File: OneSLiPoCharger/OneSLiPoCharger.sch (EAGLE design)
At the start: 16 parts, among them IC1 LM358N, Q1 BUZ10

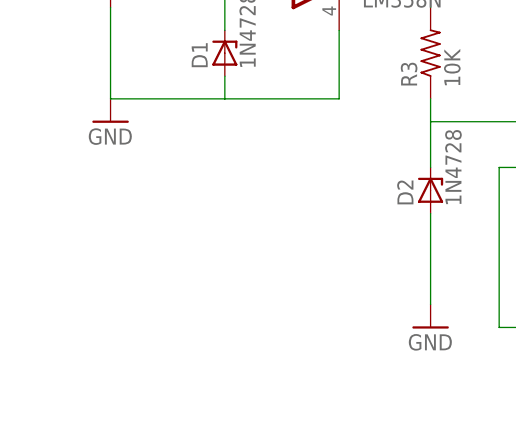
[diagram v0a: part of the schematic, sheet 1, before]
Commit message: Add XT60 to schematic
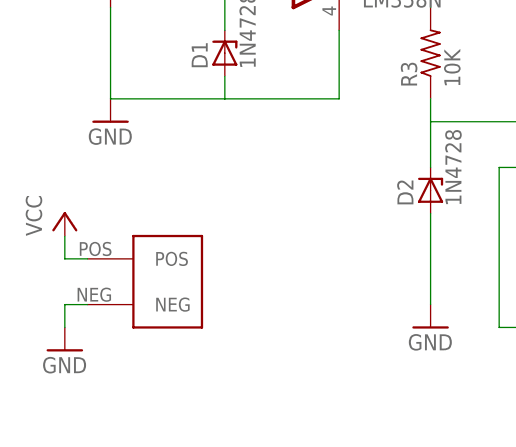
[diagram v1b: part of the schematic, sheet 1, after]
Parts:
- added U$3: XT60, XTConnector:XT60
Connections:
- net GND: now also U$3.NEG
- net VCC: now also U$3.POS
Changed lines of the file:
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@@
 <part name="C3" library="rcl" deviceset="C-US" device="C0805" value="4.7uF"/>
 <part name="GND6" library="supply1" deviceset="GND" device=""/>
+<part name="U$3" library="XTConnector" deviceset="XT60" device=""/>
+<part name="GND7" library="supply1" deviceset="GND" device=""/>
+<part name="P+5" library="supply1" deviceset="VCC" device=""/>
 </parts>
 <sheets>
@@
 <instance part="P+2" gate="VCC" x="101.6" y="33.02"/>
 <instance part="P+3" gate="1" x="116.84" y="27.94"/>
+<instance part="U$3" gate="G$1" x="20.32" y="5.08"/>
+<instance part="GND7" gate="1" x="17.78" y="-2.54"/>
+<instance part="P+5" gate="VCC" x="17.78" y="12.7"/>
 </instances>
 <busses>
@@
 <wire x1="101.6" y1="25.4" x2="101.6" y2="30.48" width="0.1524" layer="91"/>
 </segment>
+<segment>
+<pinref part="P+5" gate="VCC" pin="VCC"/>
+<pinref part="U$3" gate="G$1" pin="POS"/>
+<wire x1="17.78" y1="10.16" x2="17.78" y2="7.62" width="0.1524" layer="91"/>
+<wire x1="17.78" y1="7.62" x2="20.32" y2="7.62" width="0.1524" layer="91"/>
+</segment>
 </net>
 <net name="GND" class="0">
@@
 <wire x1="109.22" y1="-5.08" x2="109.22" y2="0" width="0.1524" layer="91"/>
 </segment>
+<segment>
+<pinref part="U$3" gate="G$1" pin="NEG"/>
+<pinref part="GND7" gate="1" pin="GND"/>
+<wire x1="20.32" y1="2.54" x2="17.78" y2="2.54" width="0.1524" layer="91"/>
+<wire x1="17.78" y1="2.54" x2="17.78" y2="0" width="0.1524" layer="91"/>
+</segment>
 </net>

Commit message: Start laying out the board
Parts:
- added LED2: (no value), led:LED3MM
- added R7: 3.9k, rcl:R-US_M0805
- R5: value (none) -> 4.7K; device rcl:R-US_M0805 -> rcl:R-US_0411/12
- R6: value 3.9k -> (none)
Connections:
- new net N$10: LED1.A, R5.1
- net +5V: now also LED2.A, R5.2; no longer LED1.A
- net GND: now also LED1.C, R7.1, U$2.P$1; no longer R6.1
- net N$6: now also LED2.C, R6.2; no longer LED1.C, R5.2
- net N$7: now also R6.1; no longer R5.1
- net N$8: now also R7.2; no longer R6.2
- net N$9: now also U$2.P$2
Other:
- moved on the sheet: R6
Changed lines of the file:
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@@
 <part name="U$1" library="MCP73831" deviceset="MCP73831" device=""/>
 <part name="P+4" library="supply1" deviceset="+5V" device=""/>
-<part name="LED1" library="led" deviceset="LED" device="3MM"/>
+<part name="LED2" library="led" deviceset="LED" device="3MM"/>
 <part name="C2" library="rcl" deviceset="C-US" device="C0805" value="4.7uF"/>
-<part name="R5" library="rcl" deviceset="R-US_" device="M0805"/>
+<part name="R6" library="rcl" deviceset="R-US_" device="M0805"/>
 <part name="GND4" library="supply1" deviceset="GND" device=""/>
 <part name="GND5" library="supply1" deviceset="GND" device=""/>
-<part name="R6" library="rcl" deviceset="R-US_" device="M0805" value="3.9k"/>
+<part name="R7" library="rcl" deviceset="R-US_" device="M0805" value="3.9k"/>
 <part name="U$2" library="Picoblade" deviceset="PICOBLADE-2PIN" device=""/>
 <part name="C3" library="rcl" deviceset="C-US" device="C0805" value="4.7uF"/>
@@
 <part name="GND7" library="supply1" deviceset="GND" device=""/>
 <part name="P+5" library="supply1" deviceset="VCC" device=""/>
+<part name="LED1" library="led" deviceset="LED" device="3MM"/>
+<part name="R5" library="rcl" deviceset="R-US_" device="0411/12" value="4.7K"/>
+<part name="P+6" library="supply1" deviceset="+5V" device=""/>
+<part name="GND8" library="supply1" deviceset="GND" device=""/>
 </parts>
 <sheets>
@@
 <instance part="GND7" gate="1" x="17.78" y="-2.54"/>
 <instance part="P+5" gate="VCC" x="17.78" y="12.7"/>
+<instance part="LED1" gate="G$1" x="88.9" y="50.8" rot="R90"/>
+<instance part="R5" gate="G$1" x="78.74" y="50.8" rot="R180"/>
+<instance part="P+6" gate="1" x="68.58" y="55.88"/>
+<instance part="GND8" gate="1" x="96.52" y="45.72"/>
 </instances>
 <busses>
@@
 <wire x1="17.78" y1="2.54" x2="17.78" y2="0" width="0.1524" layer="91"/>
 </segment>
+<segment>
+<pinref part="LED1" gate="G$1" pin="C"/>
+<pinref part="GND8" gate="1" pin="GND"/>
+<wire x1="93.98" y1="50.8" x2="96.52" y2="50.8" width="0.1524" layer="91"/>
+<wire x1="96.52" y1="50.8" x2="96.52" y2="48.26" width="0.1524" layer="91"/>
+</segment>
 </net>
 <net name="N$1" class="0">
@@
 <wire x1="116.84" y1="20.32" x2="116.84" y2="25.4" width="0.1524" layer="91"/>
 </segment>
+<segment>
+<pinref part="P+6" gate="1" pin="+5V"/>
+<pinref part="R5" gate="G$1" pin="2"/>
+<wire x1="68.58" y1="53.34" x2="68.58" y2="50.8" width="0.1524" layer="91"/>
+<wire x1="68.58" y1="50.8" x2="73.66" y2="50.8" width="0.1524" layer="91"/>
+</segment>
+</net>
+<net name="N$10" class="0">
+<segment>
+<pinref part="R5" gate="G$1" pin="1"/>
+<pinref part="LED1" gate="G$1" pin="A"/>
+<wire x1="83.82" y1="50.8" x2="86.36" y2="50.8" width="0.1524" layer="91"/>
+</segment>
 </net>
 </nets>
@@
 <instance part="U$1" gate="G$1" x="35.56" y="48.26"/>
 <instance part="P+4" gate="1" x="7.62" y="58.42"/>
-<instance part="LED1" gate="G$1" x="15.24" y="48.26"/>
+<instance part="LED2" gate="G$1" x="15.24" y="48.26"/>
 <instance part="C2" gate="G$1" x="7.62" y="48.26"/>
-<instance part="R5" gate="G$1" x="15.24" y="35.56" rot="R90"/>
+<instance part="R6" gate="G$1" x="15.24" y="35.56" rot="R90"/>
 <instance part="GND4" gate="1" x="7.62" y="38.1"/>
 <instance part="GND5" gate="1" x="48.26" y="33.02"/>
-<instance part="R6" gate="G$1" x="48.26" y="43.18" rot="R90"/>
+<instance part="R7" gate="G$1" x="48.26" y="43.18" rot="R90"/>
 <instance part="U$2" gate="G$1" x="58.42" y="55.88" rot="R180"/>
 <instance part="C3" gate="G$1" x="43.18" y="63.5"/>
@@
 <net name="+5V" class="0">
 <segment>
-<pinref part="LED1" gate="G$1" pin="A"/>
+<pinref part="LED2" gate="G$1" pin="A"/>
 <wire x1="15.24" y1="50.8" x2="15.24" y2="53.34" width="0.1524" layer="91"/>
 <pinref part="C2" gate="G$1" pin="1"/>
@@
 <net name="N$6" class="0">
 <segment>
-<pinref part="LED1" gate="G$1" pin="C"/>
-<pinref part="R5" gate="G$1" pin="2"/>
+<pinref part="LED2" gate="G$1" pin="C"/>
+<pinref part="R6" gate="G$1" pin="2"/>
 <wire x1="15.24" y1="43.18" x2="15.24" y2="40.64" width="0.1524" layer="91"/>
 </segment>
@@
 <net name="N$7" class="0">
 <segment>
-<pinref part="R5" gate="G$1" pin="1"/>
+<pinref part="R6" gate="G$1" pin="1"/>
 <wire x1="15.24" y1="30.48" x2="20.32" y2="30.48" width="0.1524" layer="91"/>
 <wire x1="20.32" y1="30.48" x2="20.32" y2="43.18" width="0.1524" layer="91"/>
@@
 </segment>
 <segment>
-<pinref part="R6" gate="G$1" pin="1"/>
+<pinref part="R7" gate="G$1" pin="1"/>
 <wire x1="43.18" y1="38.1" x2="48.26" y2="38.1" width="0.1524" layer="91"/>
 <pinref part="GND5" gate="1" pin="GND"/>
@@
 <pinref part="C3" gate="G$1" pin="1"/>
 <wire x1="43.18" y1="68.58" x2="43.18" y2="66.04" width="0.1524" layer="91"/>
-<wire x1="43.18" y1="66.04" x2="53.34" y2="66.04" width="0.1524" layer="91"/>
-<wire x1="53.34" y1="66.04" x2="53.34" y2="58.42" width="0.1524" layer="91"/>
+<wire x1="43.18" y1="66.04" x2="50.8" y2="66.04" width="0.1524" layer="91"/>
+<pinref part="U$2" gate="G$1" pin="P$1"/>
+<wire x1="50.8" y1="66.04" x2="50.8" y2="58.42" width="0.1524" layer="91"/>
 </segment>
 </net>
@@
 <segment>
 <pinref part="U$1" gate="G$1" pin="PROG"/>
-<pinref part="R6" gate="G$1" pin="2"/>
+<pinref part="R7" gate="G$1" pin="2"/>
 <wire x1="43.18" y1="48.26" x2="48.26" y2="48.26" width="0.1524" layer="91"/>
 </segment>
@@
 <pinref part="U$1" gate="G$1" pin="VBAT"/>
 <wire x1="43.18" y1="58.42" x2="43.18" y2="53.34" width="0.1524" layer="91"/>
-<wire x1="43.18" y1="53.34" x2="53.34" y2="53.34" width="0.1524" layer="91"/>
-</segment>
-</net>
+<pinref part="U$2" gate="G$1" pin="P$2"/>
+<wire x1="43.18" y1="53.34" x2="50.8" y2="53.34" width="0.1524" layer="91"/>
+</segment>
+</net>

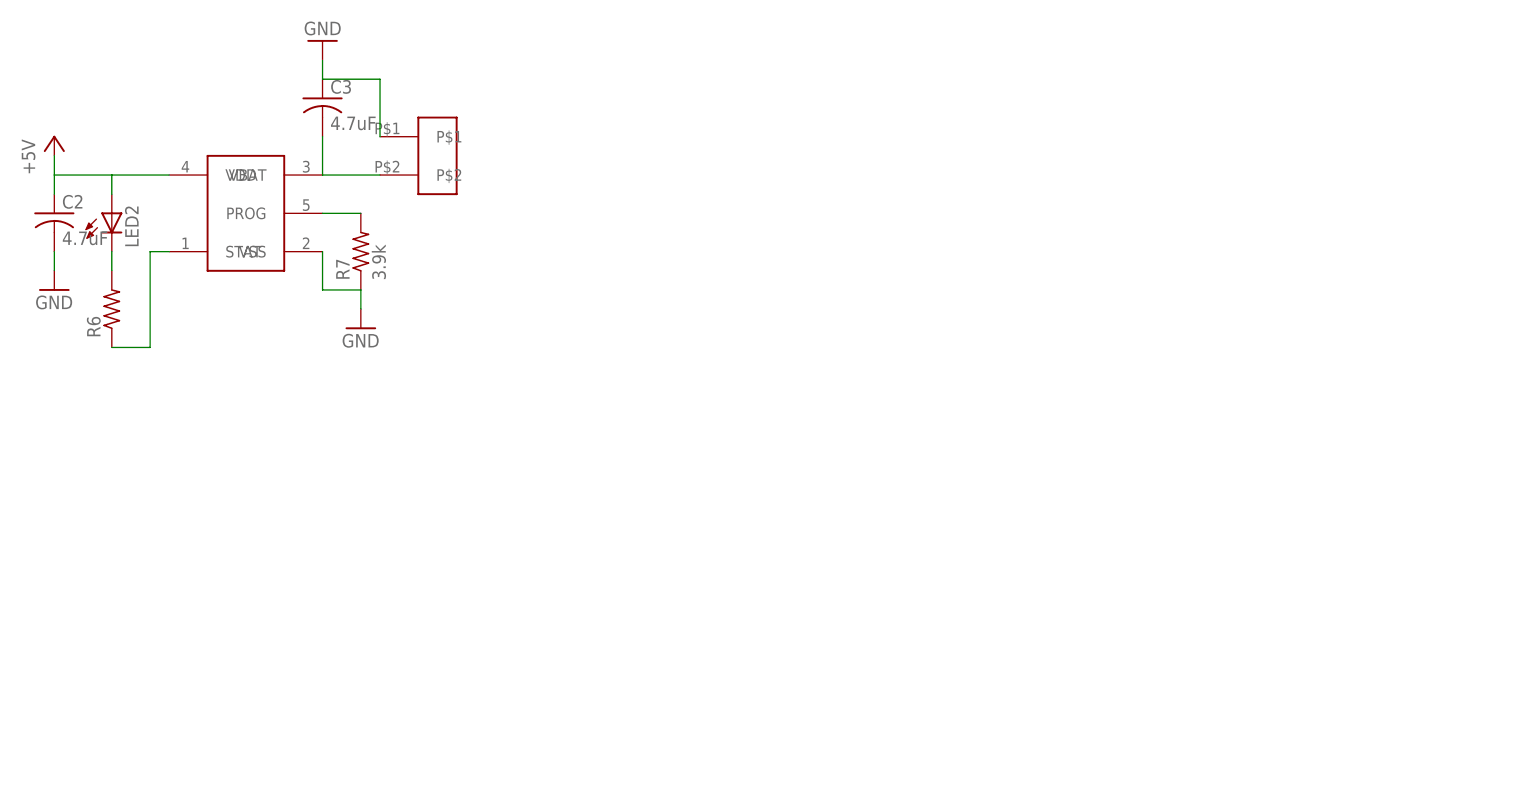
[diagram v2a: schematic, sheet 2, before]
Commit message: Add all charger circuits
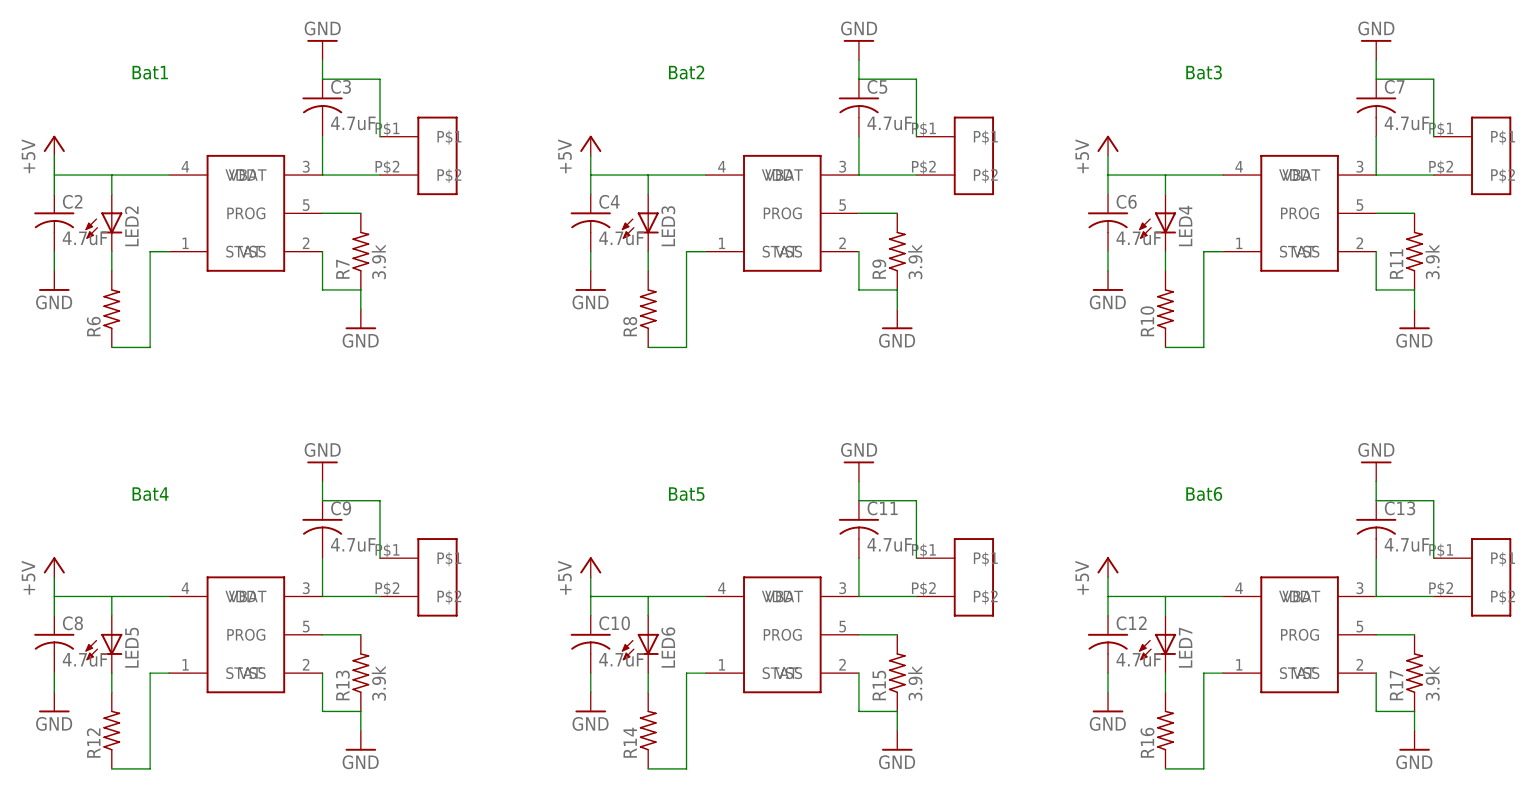
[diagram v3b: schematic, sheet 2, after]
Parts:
- added C10, C11, C12, C13, C4, C5, C6, C7, C8, C9: 4.7uF, rcl:C-USC0805
- added LED3, LED4, LED5, LED6, LED7: (no value), led:LED3MM
- added R10, R12, R14, R16, R8: (no value), rcl:R-US_M0805
- added R11, R13, R15, R17, R9: 3.9k, rcl:R-US_M0805
- added U$10, U$12, U$4, U$6, U$8: MCP73831, MCP73831:MCP73831
- added U$11, U$13, U$5, U$7, U$9: PICOBLADE-2PIN, Picoblade:PICOBLADE-2PIN
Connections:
- new net N$11: LED3.C, R8.2
- new net N$12: R8.1, U$4.STAT
- new net N$13: R9.2, U$4.PROG
- new net N$14: C5.2, U$4.VBAT, U$5.P$2
- new net N$15: LED4.C, R10.2
- new net N$16: R10.1, U$6.STAT
- new net N$17: R11.2, U$6.PROG
- new net N$18: C7.2, U$6.VBAT, U$7.P$2
- new net N$19: LED5.C, R12.2
- new net N$20: R12.1, U$8.STAT
- new net N$21: R13.2, U$8.PROG
- new net N$22: C9.2, U$8.VBAT, U$9.P$2
- new net N$23: LED6.C, R14.2
- new net N$24: R14.1, U$10.STAT
- new net N$25: R15.2, U$10.PROG
- new net N$26: C11.2, U$10.VBAT, U$11.P$2
- new net N$27: LED7.C, R16.2
- new net N$28: R16.1, U$12.STAT
- new net N$29: R17.2, U$12.PROG
- new net N$30: C13.2, U$12.VBAT, U$13.P$2
- net +5V: now also C10.1, C12.1, C4.1, C6.1, C8.1, LED3.A, LED4.A, LED5.A, LED6.A, LED7.A, U$10.VDD, U$12.VDD, U$4.VDD, U$6.VDD, U$8.VDD
- net GND: now also C10.2, C11.1, C12.2, C13.1, C4.2, C5.1, C6.2, C7.1, C8.2, C9.1, R11.1, R13.1, R15.1, R17.1, R9.1, U$10.VSS, U$11.P$1, U$12.VSS, U$13.P$1, U$4.VSS, U$5.P$1, U$6.VSS, U$7.P$1, U$8.VSS, U$9.P$1
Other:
- note added: "Bat1"
- note added: "Bat2"
- note added: "Bat3"
- note added: "Bat4"
- note added: "Bat5"
- note added: "Bat6"

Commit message: Schematic update.
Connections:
- net GND renamed N$50
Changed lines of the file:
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@@
 </segment>
 </net>
-<net name="GND" class="0">
+<net name="N$50" class="0">
 <segment>
 <pinref part="R1" gate="G$1" pin="A"/>
@@
 </segment>
 </net>
-<net name="GND" class="0">
+<net name="N$50" class="0">
 <segment>
 <pinref part="C2" gate="G$1" pin="2"/>

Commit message: Pull in updates to Picoblade library
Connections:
- net N$50 renamed GND
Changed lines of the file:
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@@
 </segment>
 </net>
-<net name="N$50" class="0">
+<net name="GND" class="0">
 <segment>
 <pinref part="R1" gate="G$1" pin="A"/>
@@
 </segment>
 </net>
-<net name="N$50" class="0">
+<net name="GND" class="0">
 <segment>
 <pinref part="C2" gate="G$1" pin="2"/>

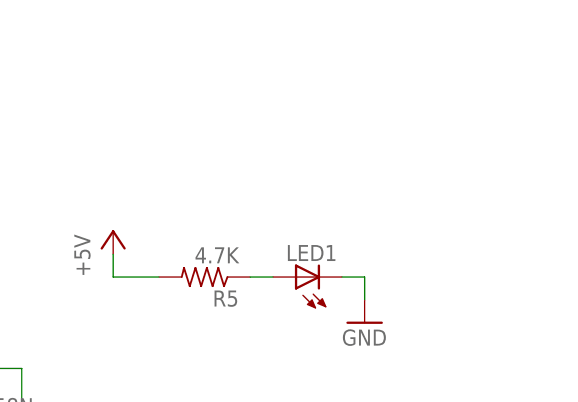
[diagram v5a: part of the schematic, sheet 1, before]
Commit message: Add a header for a voltmeter module.
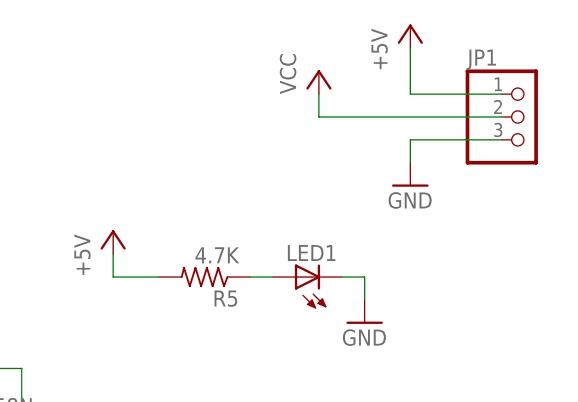
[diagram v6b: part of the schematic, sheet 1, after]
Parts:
- added JP1: (no value), pinhead:PINHD-1X3
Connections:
- net +5V: now also JP1.1
- net GND: now also JP1.3
- net VCC: now also JP1.2
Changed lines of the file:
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@@
 <part name="C13" library="rcl" deviceset="C-US" device="C0805" value="4.7uF"/>
 <part name="GND23" library="supply1" deviceset="GND" device=""/>
+<part name="JP1" library="pinhead" deviceset="PINHD-1X3" device=""/>
+<part name="GND24" library="supply1" deviceset="GND" device=""/>
+<part name="P+12" library="supply1" deviceset="+5V" device=""/>
+<part name="P+13" library="supply1" deviceset="VCC" device=""/>
 </parts>
 <sheets>
@@
 <instance part="P+6" gate="1" x="68.58" y="55.88"/>
 <instance part="GND8" gate="1" x="96.52" y="45.72"/>
+<instance part="JP1" gate="A" x="114.3" y="68.58"/>
+<instance part="GND24" gate="1" x="101.6" y="60.96"/>
+<instance part="P+12" gate="1" x="101.6" y="78.74"/>
+<instance part="P+13" gate="VCC" x="91.44" y="73.66"/>
 </instances>
 <busses>
@@
 <wire x1="17.78" y1="10.16" x2="17.78" y2="7.62" width="0.1524" layer="91"/>
 <wire x1="17.78" y1="7.62" x2="20.32" y2="7.62" width="0.1524" layer="91"/>
+</segment>
+<segment>
+<pinref part="JP1" gate="A" pin="2"/>
+<pinref part="P+13" gate="VCC" pin="VCC"/>
+<wire x1="111.76" y1="68.58" x2="91.44" y2="68.58" width="0.1524" layer="91"/>
+<wire x1="91.44" y1="68.58" x2="91.44" y2="71.12" width="0.1524" layer="91"/>
 </segment>
 </net>
@@
 <wire x1="93.98" y1="50.8" x2="96.52" y2="50.8" width="0.1524" layer="91"/>
 <wire x1="96.52" y1="50.8" x2="96.52" y2="48.26" width="0.1524" layer="91"/>
+</segment>
+<segment>
+<pinref part="JP1" gate="A" pin="3"/>
+<pinref part="GND24" gate="1" pin="GND"/>
+<wire x1="111.76" y1="66.04" x2="101.6" y2="66.04" width="0.1524" layer="91"/>
+<wire x1="101.6" y1="66.04" x2="101.6" y2="63.5" width="0.1524" layer="91"/>
 </segment>
 </net>
@@
 <wire x1="68.58" y1="50.8" x2="73.66" y2="50.8" width="0.1524" layer="91"/>
 </segment>
+<segment>
+<pinref part="P+12" gate="1" pin="+5V"/>
+<wire x1="101.6" y1="76.2" x2="101.6" y2="71.12" width="0.1524" layer="91"/>
+<pinref part="JP1" gate="A" pin="1"/>
+<wire x1="101.6" y1="71.12" x2="111.76" y2="71.12" width="0.1524" layer="91"/>
+</segment>
 </net>

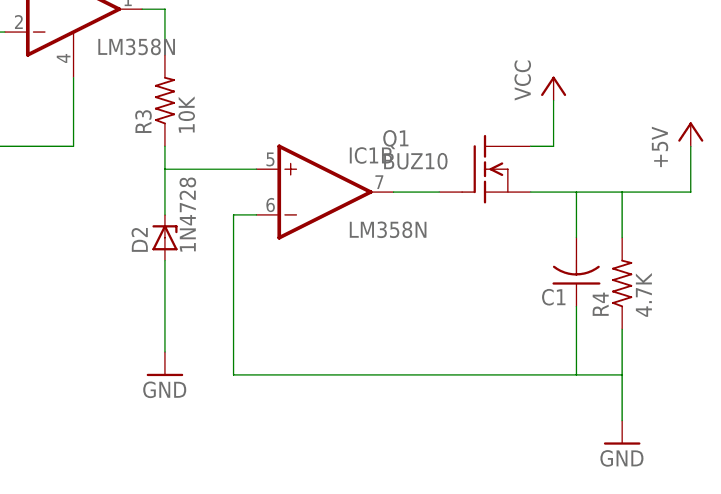
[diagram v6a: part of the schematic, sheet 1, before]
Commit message: Prep board for OSHPark. Fix feedback on voltage regulator opamp.
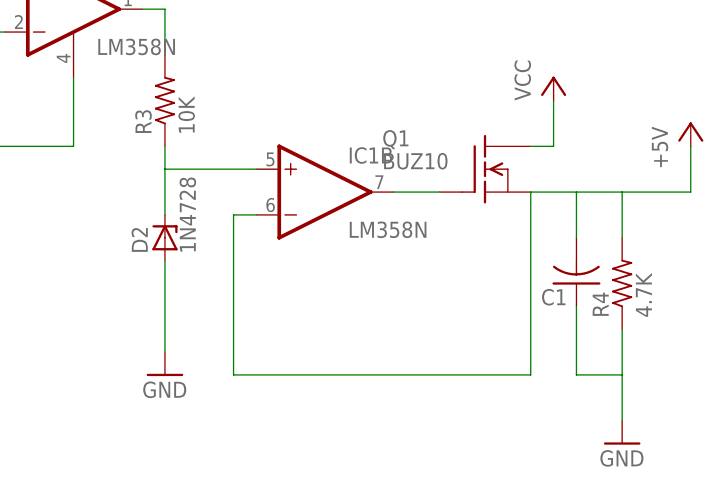
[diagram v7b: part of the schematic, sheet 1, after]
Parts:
- R2, R3, R4, R5: device rcl:R-US_0411/12 -> rcl:R-US_0207/10
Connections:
- net +5V: now also IC1B.-IN
- net GND: no longer IC1B.-IN
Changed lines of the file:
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@@
 <part name="GND1" library="supply1" deviceset="GND" device=""/>
 <part name="D1" library="diode" deviceset="1N4728" device=""/>
-<part name="R2" library="rcl" deviceset="R-US_" device="0411/12" value="1K"/>
+<part name="R2" library="rcl" deviceset="R-US_" device="0207/10" value="1K"/>
 <part name="D2" library="diode" deviceset="1N4728" device=""/>
-<part name="R3" library="rcl" deviceset="R-US_" device="0411/12" value="10K"/>
+<part name="R3" library="rcl" deviceset="R-US_" device="0207/10" value="10K"/>
 <part name="GND2" library="supply1" deviceset="GND" device=""/>
-<part name="R4" library="rcl" deviceset="R-US_" device="0411/12" value="4.7K"/>
+<part name="R4" library="rcl" deviceset="R-US_" device="0207/10" value="4.7K"/>
 <part name="C1" library="rcl" deviceset="C-US" device="025-025X050"/>
 <part name="GND3" library="supply1" deviceset="GND" device=""/>
@@
 <part name="P+5" library="supply1" deviceset="VCC" device=""/>
 <part name="LED1" library="led" deviceset="LED" device="3MM"/>
-<part name="R5" library="rcl" deviceset="R-US_" device="0411/12" value="4.7K"/>
+<part name="R5" library="rcl" deviceset="R-US_" device="0207/10" value="4.7K"/>
 <part name="P+6" library="supply1" deviceset="+5V" device=""/>
 <part name="GND8" library="supply1" deviceset="GND" device=""/>
@@
 </segment>
 <segment>
-<pinref part="IC1" gate="B" pin="-IN"/>
-<wire x1="68.58" y1="17.78" x2="66.04" y2="17.78" width="0.1524" layer="91"/>
-<wire x1="66.04" y1="17.78" x2="66.04" y2="0" width="0.1524" layer="91"/>
 <pinref part="C1" gate="G$1" pin="1"/>
-<wire x1="66.04" y1="0" x2="104.14" y2="0" width="0.1524" layer="91"/>
 <wire x1="104.14" y1="0" x2="104.14" y2="7.62" width="0.1524" layer="91"/>
 <pinref part="R4" gate="G$1" pin="1"/>
@@
 <pinref part="P+3" gate="1" pin="+5V"/>
 <wire x1="116.84" y1="20.32" x2="116.84" y2="25.4" width="0.1524" layer="91"/>
-</segment>
-<segment>
+<wire x1="99.06" y1="20.32" x2="99.06" y2="0" width="0.1524" layer="91"/>
+<pinref part="IC1" gate="B" pin="-IN"/>
+<wire x1="68.58" y1="17.78" x2="66.04" y2="17.78" width="0.1524" layer="91"/>
+<wire x1="66.04" y1="17.78" x2="66.04" y2="0" width="0.1524" layer="91"/>
+<wire x1="99.06" y1="0" x2="66.04" y2="0" width="0.1524" layer="91"/>
+</segment>
+<segment>
